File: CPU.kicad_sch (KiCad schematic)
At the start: 56 parts, among them Y1 X322524MKB4SI

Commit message: Пытаюсь сделать трассировку DDК
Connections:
- net SDQ31: no longer DD1.L15 (SZQ)
- net VCC-DRAM: now also DD1.L9 (VCC_DRAM_1)
- net at R31.1: now also DD1.L15 (SZQ); no longer DD1.L9 (VCC_DRAM_1)
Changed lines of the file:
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@@
 	)
 	(junction
+		(at 369.57 149.86)
+		(diameter 0)
+		(color 0 0 0 0)
+	)
+	(junction
 		(at 260.35 228.6)
 		(diameter 0)
@@
 	(wire
 		(pts
+			(xy 369.57 147.32) (xy 369.57 149.86)
+		)
+		(stroke
+			(width 0)
+			(type default)
+		)
+	)
+	(wire
+		(pts
 			(xy 254 228.6) (xy 260.35 228.6)
 		)
@@
 	(wire
 		(pts
+			(xy 367.03 147.32) (xy 369.57 147.32)
+		)
+		(stroke
+			(width 0)
+			(type default)
+		)
+	)
+	(wire
+		(pts
 			(xy 128.27 68.58) (xy 125.73 68.58)
 		)
@@
 	(wire
 		(pts
+			(xy 381 146.05) (xy 381 144.78)
+		)
+		(stroke
+			(width 0)
+			(type default)
+		)
+	)
+	(wire
+		(pts
 			(xy 128.27 83.82) (xy 125.73 83.82)
 		)
@@
 	(wire
 		(pts
-			(xy 381 148.59) (xy 381 147.32)
-		)
-		(stroke
-			(width 0)
-			(type default)
-		)
-	)
-	(wire
-		(pts
 			(xy 367.03 78.74) (xy 369.57 78.74)
 		)
@@
 	(wire
 		(pts
-			(xy 381 147.32) (xy 377.19 147.32)
-		)
-		(stroke
-			(width 0)
-			(type default)
-		)
-	)
-	(wire
-		(pts
 			(xy 86.36 209.55) (xy 80.01 209.55)
 		)
@@
 	(wire
 		(pts
+			(xy 381 144.78) (xy 377.19 144.78)
+		)
+		(stroke
+			(width 0)
+			(type default)
+		)
+	)
+	(wire
+		(pts
 			(xy 66.04 180.34) (xy 77.47 180.34)
 		)
@@
 	(wire
 		(pts
-			(xy 80.01 222.25) (xy 80.01 220.98)
+			(xy 367.03 144.78) (xy 369.57 144.78)
 		)
 		(stroke
@@
 	(wire
 		(pts
-			(xy 74.93 167.64) (xy 77.47 167.64)
+			(xy 80.01 222.25) (xy 80.01 220.98)
 		)
 		(stroke
@@
 	(wire
 		(pts
-			(xy 193.04 259.08) (xy 193.04 257.81)
+			(xy 74.93 167.64) (xy 77.47 167.64)
 		)
 		(stroke
@@
 	(wire
 		(pts
-			(xy 128.27 132.08) (xy 125.73 132.08)
+			(xy 193.04 259.08) (xy 193.04 257.81)
 		)
 		(stroke
@@
 	(wire
 		(pts
-			(xy 109.22 209.55) (xy 114.3 209.55)
+			(xy 128.27 132.08) (xy 125.73 132.08)
 		)
 		(stroke
@@
 	(wire
 		(pts
-			(xy 345.44 210.82) (xy 339.09 210.82)
+			(xy 109.22 209.55) (xy 114.3 209.55)
 		)
 		(stroke
@@
 	(wire
 		(pts
-			(xy 247.65 118.11) (xy 250.19 118.11)
+			(xy 345.44 210.82) (xy 339.09 210.82)
 		)
 		(stroke
@@
 	(wire
 		(pts
-			(xy 367.03 147.32) (xy 369.57 147.32)
+			(xy 247.65 118.11) (xy 250.19 118.11)
 		)
 		(stroke
@@
 	(wire
 		(pts
-			(xy 367.03 144.78) (xy 369.57 144.78)
-		)
-		(stroke
-			(width 0)
-			(type default)
-		)
-	)
-	(wire
-		(pts
 			(xy 234.95 227.33) (xy 234.95 228.6)
 		)
@@
 		)
 	)
-	(global_label "SDQ31"
-		(shape input)
-		(at 369.57 144.78 0)
-		(fields_autoplaced yes)
-		(effects
-			(font
-				(size 1.27 1.27)
-			)
-			(justify left)
-		)
-		(property "Intersheetrefs" "${INTERSHEET_REFS}"
-			(at 375.5413 144.78 0)
-			(effects
-				(font
-					(size 1.27 1.27)
-				)
-				(justify left)
-				(hide yes)
-			)
-		)
-	)
 	(global_label "SDQ30"
 		(shape input)
@@
 	)
 	(symbol
+		(lib_id "power:Earth")
+		(at 381 146.05 0)
+		(unit 1)
+		(exclude_from_sim no)
+		(in_bom yes)
+		(on_board yes)
+		(dnp no)
+		(fields_autoplaced yes)
+		(property "Reference" "#PWR0135"
+			(at 381 152.4 0)
+			(effects
+				(font
+					(size 1.27 1.27)
+				)
+				(hide yes)
+			)
+		)
+		(property "Value" "Earth"
+			(at 381 151.13 0)
+			(effects
+				(font
+					(size 1.27 1.27)
+				)
+				(hide yes)
+			)
+		)
+		(property "Footprint" ""
+			(at 381 146.05 0)
+			(effects
+				(font
+					(size 1.27 1.27)
+				)
+				(hide yes)
+			)
+		)
+		(property "Datasheet" "~"
+			(at 381 146.05 0)
+			(effects
+				(font
+					(size 1.27 1.27)
+				)
+				(hide yes)
+			)
+		)
+		(property "Description" "Power symbol creates a global label with name \"Earth\""
+			(at 381 146.05 0)
+			(effects
+				(font
+					(size 1.27 1.27)
+				)
+				(hide yes)
+			)
+		)
+		(pin "1"
+		)
+		(instances
+			(project "Sodimm-force"
+				(path "/b3673bfd-24d8-4789-b63c-c3654dc2bb6e/7bdf4494-d64d-40da-b2e3-dae4f35a6c46"
+					(reference "#PWR0135")
+					(unit 1)
+				)
+			)
+		)
+	)
+	(symbol
 		(lib_id "power:+3V8")
 		(at 339.09 201.93 0)
@@
 	(symbol
 		(lib_id "power:Earth")
-		(at 381 148.59 0)
-		(unit 1)
-		(exclude_from_sim no)
-		(in_bom yes)
-		(on_board yes)
-		(dnp no)
-		(fields_autoplaced yes)
-		(property "Reference" "#PWR0135"
-			(at 381 154.94 0)
-			(effects
-				(font
-					(size 1.27 1.27)
-				)
-				(hide yes)
-			)
-		)
-		(property "Value" "Earth"
-			(at 381 153.67 0)
-			(effects
-				(font
-					(size 1.27 1.27)
-				)
-				(hide yes)
-			)
-		)
-		(property "Footprint" ""
-			(at 381 148.59 0)
-			(effects
-				(font
-					(size 1.27 1.27)
-				)
-				(hide yes)
-			)
-		)
-		(property "Datasheet" "~"
-			(at 381 148.59 0)
-			(effects
-				(font
-					(size 1.27 1.27)
-				)
-				(hide yes)
-			)
-		)
-		(property "Description" "Power symbol creates a global label with name \"Earth\""
-			(at 381 148.59 0)
-			(effects
-				(font
-					(size 1.27 1.27)
-				)
-				(hide yes)
-			)
-		)
-		(pin "1"
-		)
-		(instances
-			(project "Sodimm-force"
-				(path "/b3673bfd-24d8-4789-b63c-c3654dc2bb6e/7bdf4494-d64d-40da-b2e3-dae4f35a6c46"
-					(reference "#PWR0135")
-					(unit 1)
-				)
-			)
-		)
-	)
-	(symbol
-		(lib_id "power:Earth")
 		(at 234.95 237.49 0)
 		(unit 1)
@@
 	)
 	(symbol
+		(lib_id "Device:R")
+		(at 373.38 144.78 90)
+		(unit 1)
+		(exclude_from_sim no)
+		(in_bom yes)
+		(on_board yes)
+		(dnp no)
+		(property "Reference" "R31"
+			(at 369.316 145.796 90)
+			(effects
+				(font
+					(size 1.27 1.27)
+				)
+			)
+		)
+		(property "Value" "20K"
+			(at 377.444 145.796 90)
+			(effects
+				(font
+					(size 1.27 1.27)
+				)
+			)
+		)
+		(property "Footprint" "Resistor_SMD:R_0402_1005Metric"
+			(at 373.38 146.558 90)
+			(effects
+				(font
+					(size 1.27 1.27)
+				)
+				(hide yes)
+			)
+		)
+		(property "Datasheet" "~"
+			(at 373.38 144.78 0)
+			(effects
+				(font
+					(size 1.27 1.27)
+				)
+				(hide yes)
+			)
+		)
+		(property "Description" "Resistor"
+			(at 373.38 144.78 0)
+			(effects
+				(font
+					(size 1.27 1.27)
+				)
+				(hide yes)
+			)
+		)
+		(pin "1"
+		)
+		(pin "2"
+		)
+		(instances
+			(project "Sodimm-force"
+				(path "/b3673bfd-24d8-4789-b63c-c3654dc2bb6e/7bdf4494-d64d-40da-b2e3-dae4f35a6c46"
+					(reference "R31")
+					(unit 1)
+				)
+			)
+		)
+	)
+	(symbol
 		(lib_id "power:+3V8")
 		(at 295.91 201.93 0)
@@
 					(unit 1)
 				)
-			)
-		)
-	)
-	(symbol
-		(lib_id "Device:R")
-		(at 373.38 147.32 90)
-		(unit 1)
-		(exclude_from_sim no)
-		(in_bom yes)
-		(on_board yes)
-		(dnp no)
-		(property "Reference" "R31"
-			(at 369.316 148.336 90)
-			(effects
-				(font
-					(size 1.27 1.27)
-				)
-			)
-		)
-		(property "Value" "20K"
-			(at 377.444 148.336 90)
-			(effects
-				(font
-					(size 1.27 1.27)
-				)
-			)
-		)
-		(property "Footprint" "Resistor_SMD:R_0402_1005Metric"
-			(at 373.38 149.098 90)
-			(effects
-				(font
-					(size 1.27 1.27)
-				)
-				(hide yes)
-			)
-		)
-		(property "Datasheet" "~"
-			(at 373.38 147.32 0)
-			(effects
-				(font
-					(size 1.27 1.27)
-				)
-				(hide yes)
-			)
-		)
-		(property "Description" "Resistor"
-			(at 373.38 147.32 0)
-			(effects
-				(font
-					(size 1.27 1.27)
-				)
-				(hide yes)
-			)
-		)
-		(pin "1"
-		)
-		(pin "2"
-		)
-		(instances
-			(project "Sodimm-force"
-				(path "/b3673bfd-24d8-4789-b63c-c3654dc2bb6e/7bdf4494-d64d-40da-b2e3-dae4f35a6c46"
-					(reference "R31")
-					(unit 1)
-				)

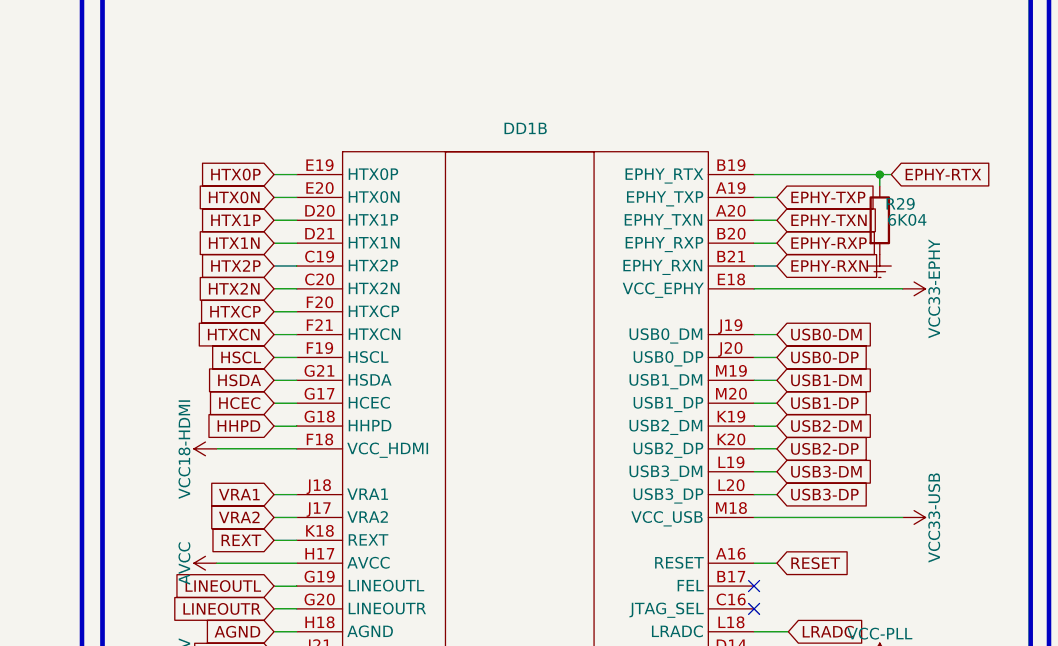
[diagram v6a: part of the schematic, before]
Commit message: Кучка исправлений, переместил SD карту, дисплей, в целом компоновка чуть другая Небольшие исправления в схеме 🤠
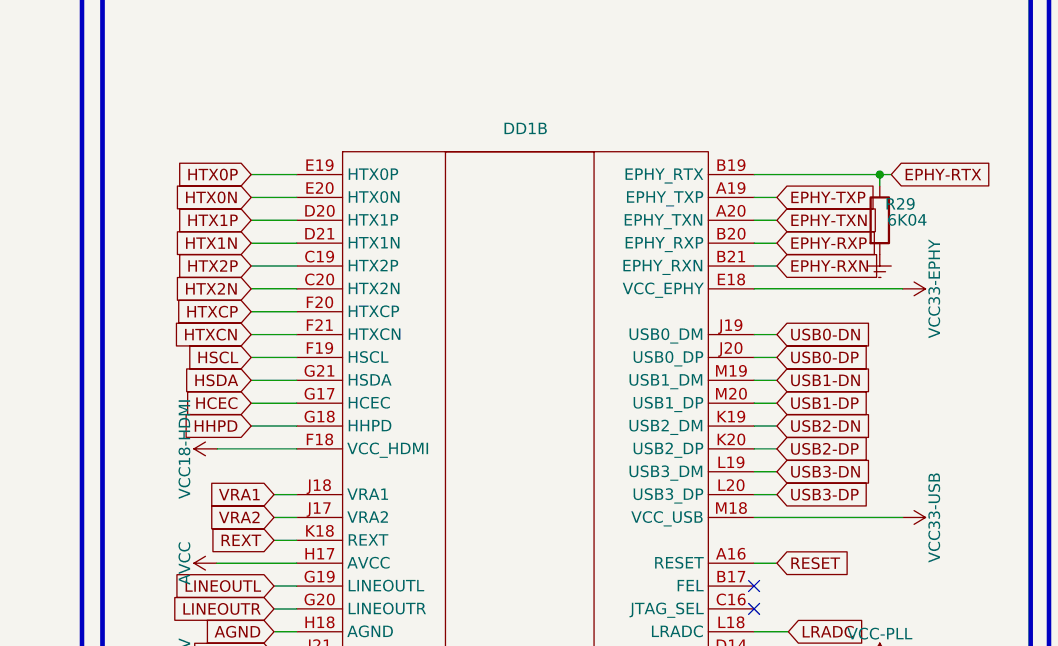
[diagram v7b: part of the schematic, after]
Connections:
- net USB0-DM renamed USB0-DN
- net USB1-DM renamed USB1-DN
- net USB2-DM renamed USB2-DN
- net USB3-DM renamed USB3-DN

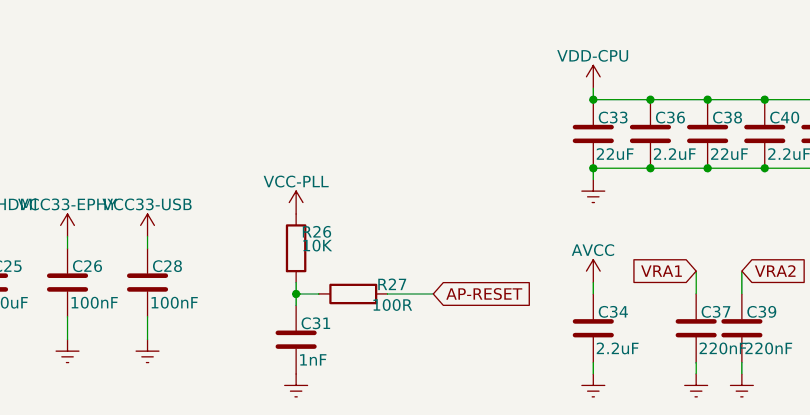
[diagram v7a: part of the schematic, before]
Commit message: Навёл красоту, убрал подтяжку для питания что скопировал с реф дизайна ( у меня не умные DC-DC ) + компоновка decoupling кондёров и быстрой обвязки чипа
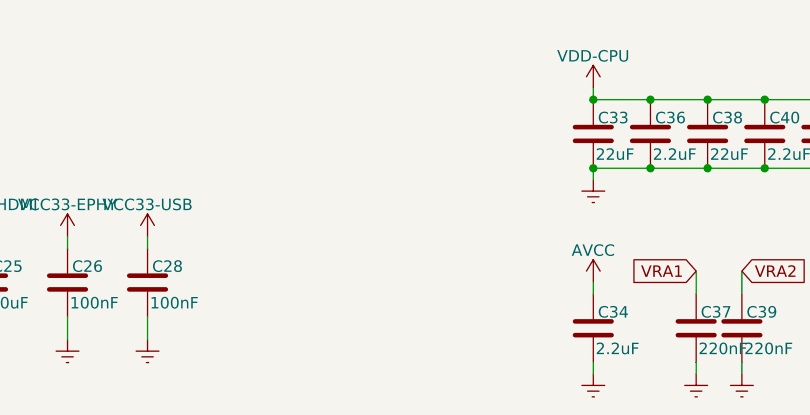
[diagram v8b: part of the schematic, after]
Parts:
- removed C31: 1nF, Capacitor_SMD:C_0402_1005Metric, symbol Device:C
- removed R26: 10K, Resistor_SMD:R_0402_1005Metric, symbol Device:R
- removed R27: 100R, Resistor_SMD:R_0402_1005Metric, symbol Device:R
